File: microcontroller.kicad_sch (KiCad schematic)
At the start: 33 parts, among them J1 Micro_SD_Card, J2 TC2030-NL, J3 USB_C_Receptacle, SW1 SW_SPST, SW2 SW_SPST, U1 W25Q128JVS, U2 STM32F411CEUx, U3 USBLC6-2SC6, Y1 8MHz, Y2 32.768KHz

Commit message: Footprint selection
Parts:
- C1, C10, C11, C12, C2, C3, C4, C5, C6, C7, C8, C9: footprint (none) -> Capacitor_SMD:C_0603_1608Metric
- D1: footprint (none) -> LED_SMD:LED_0603_1608Metric
- D2: footprint (none) -> LED_SMD:LED_RGB_5050-6
- J1: footprint (none) -> Connector_Card:microSD_HC_Molex_47219-2001
- J3: footprint (none) -> Connector_USB:USB_C_Receptacle_GCT_USB4105-xx-A_16P_TopMnt_Horizontal
- R1, R2, R3, R4, R5, R6, R7, R8, R9: footprint (none) -> Resistor_SMD:R_0603_1608Metric
- SW1, SW2: footprint (none) -> Button_Switch_SMD:SW_SPST_B3U-1000P-B
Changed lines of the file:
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@@
 			)
 		)
-		(property "Footprint" ""
+		(property "Footprint" "Capacitor_SMD:C_0603_1608Metric"
 			(at 151.13 40.64 0)
 			(effects
@@
 			)
 		)
-		(property "Footprint" ""
+		(property "Footprint" "Capacitor_SMD:C_0603_1608Metric"
 			(at 157.48 40.64 0)
 			(effects
@@
 			)
 		)
-		(property "Footprint" ""
+		(property "Footprint" "Capacitor_SMD:C_0603_1608Metric"
 			(at 125.73 40.64 0)
 			(effects
@@
 			)
 		)
-		(property "Footprint" ""
+		(property "Footprint" "Capacitor_SMD:C_0603_1608Metric"
 			(at 137.16 144.78 0)
 			(effects
@@
 			)
 		)
-		(property "Footprint" ""
+		(property "Footprint" "Capacitor_SMD:C_0603_1608Metric"
 			(at 119.38 40.64 0)
 			(effects
@@
 			)
 		)
-		(property "Footprint" ""
+		(property "Footprint" "Capacitor_SMD:C_0603_1608Metric"
 			(at 132.08 40.64 0)
 			(effects
@@
 			)
 		)
-		(property "Footprint" ""
+		(property "Footprint" "Resistor_SMD:R_0603_1608Metric"
 			(at 233.934 133.604 90)
 			(effects
@@
 			)
 		)
-		(property "Footprint" ""
+		(property "Footprint" "Capacitor_SMD:C_0603_1608Metric"
 			(at 205.74 92.71 0)
 			(effects
@@
 			)
 		)
-		(property "Footprint" ""
+		(property "Footprint" "Capacitor_SMD:C_0603_1608Metric"
 			(at 205.74 46.99 0)
 			(effects
@@
 			)
 		)
-		(property "Footprint" ""
+		(property "Footprint" "Connector_Card:microSD_HC_Molex_47219-2001"
 			(at 265.43 87.63 0)
 			(effects
@@
 			)
 		)
-		(property "Footprint" ""
+		(property "Footprint" "Resistor_SMD:R_0603_1608Metric"
 			(at 233.934 123.444 90)
 			(effects
@@
 			)
 		)
-		(property "Footprint" ""
+		(property "Footprint" "Button_Switch_SMD:SW_SPST_B3U-1000P-B"
 			(at 35.56 106.68 0)
 			(effects
@@
 			)
 		)
-		(property "Footprint" ""
+		(property "Footprint" "Resistor_SMD:R_0603_1608Metric"
 			(at 113.284 90.424 90)
 			(effects
@@
 			)
 		)
-		(property "Footprint" ""
+		(property "Footprint" "Resistor_SMD:R_0603_1608Metric"
 			(at 37.084 111.506 90)
 			(effects
@@
 			)
 		)
-		(property "Footprint" ""
+		(property "Footprint" "Resistor_SMD:R_0603_1608Metric"
 			(at 52.324 170.434 90)
 			(effects
@@
 			)
 		)
-		(property "Footprint" ""
+		(property "Footprint" "Resistor_SMD:R_0603_1608Metric"
 			(at 251.714 94.234 90)
 			(effects
@@
 			)
 		)
-		(property "Footprint" ""
+		(property "Footprint" "Capacitor_SMD:C_0603_1608Metric"
 			(at 144.78 40.64 0)
 			(effects
@@
 			)
 		)
-		(property "Footprint" ""
+		(property "Footprint" "Button_Switch_SMD:SW_SPST_B3U-1000P-B"
 			(at 38.1 81.28 0)
 			(effects
@@
 			)
 		)
-		(property "Footprint" ""
+		(property "Footprint" "Capacitor_SMD:C_0603_1608Metric"
 			(at 198.12 92.71 0)
 			(effects
@@
 			)
 		)
-		(property "Footprint" ""
+		(property "Footprint" "Resistor_SMD:R_0603_1608Metric"
 			(at 52.324 172.974 90)
 			(effects
@@
 			)
 		)
-		(property "Footprint" ""
+		(property "Footprint" "LED_SMD:LED_RGB_5050-6"
 			(at 242.57 130.81 0)
 			(effects
@@
 			)
 		)
-		(property "Footprint" ""
+		(property "Footprint" "Resistor_SMD:R_0603_1608Metric"
 			(at 251.714 96.774 90)
 			(effects
@@
 			)
 		)
-		(property "Footprint" ""
+		(property "Footprint" "Capacitor_SMD:C_0603_1608Metric"
 			(at 138.43 40.64 0)
 			(effects
@@
 			)
 		)
-		(property "Footprint" ""
+		(property "Footprint" "LED_SMD:LED_0603_1608Metric"
 			(at 120.65 91.44 0)
 			(effects
@@
 			)
 		)
-		(property "Footprint" ""
+		(property "Footprint" "Resistor_SMD:R_0603_1608Metric"
 			(at 233.934 128.524 90)
 			(effects
@@
 			)
 		)
-		(property "Footprint" ""
+		(property "Footprint" "Connector_USB:USB_C_Receptacle_GCT_USB4105-xx-A_16P_TopMnt_Horizontal"
 			(at 36.83 161.29 0)
 			(effects
@@
 			)
 		)
-		(property "Footprint" ""
+		(property "Footprint" "Capacitor_SMD:C_0603_1608Metric"
 			(at 38.1 85.09 0)
 			(effects

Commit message: Connected radio
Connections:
- net EN_RADIO is gone; now on net INT_RADIO: U2.41 (PB5)
- net INT_RADIO: no longer U2.40 (PB4)
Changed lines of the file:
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@@
-		)
-	)
-	(hierarchical_label "INT_RADIO"
-		(shape input)
-		(at 137.16 111.76 180)
-		(effects
-			(font
-				(size 1.27 1.27)
-			)
-			(justify right)
 		)
 	)
@@
 		)
 	)
-	(hierarchical_label "CS_RADIO"
-		(shape output)
-		(at 137.16 119.38 180)
+	(hierarchical_label "INT_RADIO"
+		(shape input)
+		(at 137.16 114.3 180)
 		(effects
 			(font
@@
 		)
 	)
-	(hierarchical_label "EN_RADIO"
+	(hierarchical_label "CS_RADIO"
 		(shape output)
-		(at 137.16 114.3 180)
+		(at 137.16 119.38 180)
 		(effects
 			(font

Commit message: PCB work
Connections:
- net CS_ACCEL: now also U2.20 (PB2); no longer U2.27 (PB14)
- net CS_IMU_AG: now also U2.10 (PA0); no longer U2.25 (PB12)
- net CS_IMU_MAG: now also U2.11 (PA1); no longer U2.26 (PB13)
- net CS_POWER: now also U2.12 (PA2); no longer U2.21 (PB10)
- net CS_RADIO: now also U2.14 (PA4); no longer U2.43 (PB7)
- net INT_RADIO: now also U2.13 (PA3); no longer U2.41 (PB5)
- net LED_BLUE: now also U2.29 (PA8); no longer U2.12 (PA2)
- net LED_GREEN: now also U2.30 (PA9); no longer U2.11 (PA1)
- net LED_RED: now also U2.31 (PA10); no longer U2.10 (PA0)
- net RST_RADIO: now also U2.21 (PB10); no longer U2.42 (PB6)
- no-connect marks 12 -> 13
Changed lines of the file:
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@@
+	)
+	(no_connect
+		(at 137.16 111.76)
+	)
+	(no_connect
+		(at 137.16 119.38)
 	)
 	(no_connect
@@
 	)
 	(no_connect
-		(at 137.16 106.68)
+		(at 137.16 134.62)
 	)
 	(no_connect
@@
 	)
 	(no_connect
-		(at 172.72 81.28)
-	)
-	(no_connect
-		(at 172.72 99.06)
-	)
-	(no_connect
-		(at 172.72 93.98)
+		(at 137.16 129.54)
 	)
 	(no_connect
@@
 	)
 	(no_connect
-		(at 172.72 83.82)
+		(at 137.16 116.84)
 	)
 	(no_connect
-		(at 172.72 96.52)
+		(at 137.16 114.3)
+	)
+	(no_connect
+		(at 137.16 132.08)
 	)
 	(no_connect
@@
 	(wire
 		(pts
+			(xy 181.61 99.06) (xy 172.72 99.06)
+		)
+		(stroke
+			(width 0)
+			(type default)
+		)
+	)
+	(wire
+		(pts
 			(xy 175.26 101.6) (xy 172.72 101.6)
 		)
@@
 	(wire
 		(pts
+			(xy 172.72 93.98) (xy 182.88 93.98)
+		)
+		(stroke
+			(width 0)
+			(type default)
+		)
+	)
+	(wire
+		(pts
+			(xy 184.15 96.52) (xy 172.72 96.52)
+		)
+		(stroke
+			(width 0)
+			(type default)
+		)
+	)
+	(wire
+		(pts
 			(xy 138.43 38.1) (xy 144.78 38.1)
 		)
@@
 	(wire
 		(pts
-			(xy 181.61 73.66) (xy 172.72 73.66)
-		)
-		(stroke
-			(width 0)
-			(type default)
-		)
-	)
-	(wire
-		(pts
 			(xy 40.64 106.68) (xy 40.64 110.49)
 		)
@@
 	(wire
 		(pts
-			(xy 172.72 78.74) (xy 182.88 78.74)
-		)
-		(stroke
-			(width 0)
-			(type default)
-		)
-	)
-	(wire
-		(pts
 			(xy 119.38 43.18) (xy 125.73 43.18)
 		)
@@
 		(pts
 			(xy 132.08 73.66) (xy 137.16 73.66)
-		)
-		(stroke
-			(width 0)
-			(type default)
-		)
-	)
-	(wire
-		(pts
-			(xy 184.15 76.2) (xy 172.72 76.2)
 		)
 		(stroke
@@
 		)
 	)
-	(label "LED_BLUE"
-		(at 182.88 78.74 180)
-		(effects
-			(font
-				(size 1.27 1.27)
-			)
-			(justify right bottom)
-		)
-	)
 	(label "SWD"
 		(at 176.53 106.68 180)
@@
 		)
 	)
-	(label "LED_RED"
-		(at 181.61 73.66 180)
-		(effects
-			(font
-				(size 1.27 1.27)
-			)
-			(justify right bottom)
-		)
-	)
 	(label "MOSI"
 		(at 218.44 100.33 0)
@@
 		)
 	)
-	(label "LED_GREEN"
-		(at 184.15 76.2 180)
-		(effects
-			(font
-				(size 1.27 1.27)
-			)
-			(justify right bottom)
-		)
-	)
 	(label "MISO"
 		(at 218.44 97.79 0)
@@
 		)
 	)
+	(label "LED_BLUE"
+		(at 182.88 93.98 180)
+		(effects
+			(font
+				(size 1.27 1.27)
+			)
+			(justify right bottom)
+		)
+	)
+	(label "LED_RED"
+		(at 181.61 99.06 180)
+		(effects
+			(font
+				(size 1.27 1.27)
+			)
+			(justify right bottom)
+		)
+	)
+	(label "LED_GREEN"
+		(at 184.15 96.52 180)
+		(effects
+			(font
+				(size 1.27 1.27)
+			)
+			(justify right bottom)
+		)
+	)
 	(label "CS_FLASH"
 		(at 217.17 40.64 0)
@@
 			)
 			(justify right bottom)
+		)
+	)
+	(hierarchical_label "CS_IMU_AG"
+		(shape output)
+		(at 172.72 73.66 0)
+		(effects
+			(font
+				(size 1.27 1.27)
+			)
+			(justify left)
+		)
+	)
+	(hierarchical_label "CS_IMU_MAG"
+		(shape output)
+		(at 172.72 76.2 0)
+		(effects
+			(font
+				(size 1.27 1.27)
+			)
+			(justify left)
+		)
+	)
+	(hierarchical_label "CS_RADIO"
+		(shape output)
+		(at 172.72 83.82 0)
+		(effects
+			(font
+				(size 1.27 1.27)
+			)
+			(justify left)
 		)
 	)
@@
 		)
 	)
-	(hierarchical_label "INT_RADIO"
-		(shape input)
-		(at 137.16 114.3 180)
-		(effects
-			(font
-				(size 1.27 1.27)
-			)
-			(justify right)
-		)
-	)
-	(hierarchical_label "CS_RADIO"
-		(shape output)
-		(at 137.16 119.38 180)
-		(effects
-			(font
-				(size 1.27 1.27)
-			)
-			(justify right)
-		)
-	)
 	(hierarchical_label "CS_POWER"
 		(shape output)
-		(at 137.16 127 180)
-		(effects
-			(font
-				(size 1.27 1.27)
-			)
-			(justify right)
-		)
-	)
-	(hierarchical_label "RST_RADIO"
-		(shape output)
-		(at 137.16 116.84 180)
+		(at 172.72 78.74 0)
+		(effects
+			(font
+				(size 1.27 1.27)
+			)
+			(justify left)
+		)
+	)
+	(hierarchical_label "CS_ACCEL"
+		(shape input)
+		(at 137.16 106.68 180)
 		(effects
 			(font
@@
 		)
 	)
-	(hierarchical_label "CS_ACCEL"
-		(shape output)
-		(at 137.16 134.62 180)
-		(effects
-			(font
-				(size 1.27 1.27)
-			)
-			(justify right)
-		)
-	)
-	(hierarchical_label "CS_IMU_MAG"
-		(shape output)
-		(at 137.16 132.08 180)
-		(effects
-			(font
-				(size 1.27 1.27)
-			)
-			(justify right)
+	(hierarchical_label "INT_RADIO"
+		(shape input)
+		(at 172.72 81.28 0)
+		(effects
+			(font
+				(size 1.27 1.27)
+			)
+			(justify left)
 		)
 	)
@@
 		)
 	)
-	(hierarchical_label "CS_IMU_AG"
+	(hierarchical_label "RST_RADIO"
 		(shape output)
-		(at 137.16 129.54 180)
-		(effects
-			(font
+		(at 137.16 127 180)
+		(effects
+			(font

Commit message: Silk updates
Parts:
- added J6: Stemma, Connector_JST:JST_SH_SM04B-SRSS-TB_1x04-1MP_P1.00mm_Horizontal, symbol Connector_Generic_Shielded:Conn_01x04_Shielded
- added R16, R17: 5.1k, Resistor_SMD:R_0603_1608Metric, symbol Device:R_US
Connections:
- net +3V3: now also J6.3 (Pin_3), R16.1, R17.1
- net GND: now also J6.4 (Pin_4), J6.SH (Shield)
- net SCL: now reaches U2.42 (PB6)
- net SCL: now also J6.1 (Pin_1), R16.2
- net SDA: now reaches U2.43 (PB7)
- net SDA: now also J6.2 (Pin_2), R17.2
- no-connect marks 13 -> 11

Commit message: Addeed part numbers
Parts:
- C1, C12: LCSC (none) -> C19666
- C10: LCSC (none) -> C96446
- C11, C3, C4, C5, C6, C7, C8, C9: LCSC (none) -> C14663
- C2: LCSC (none) -> C15849
- D1: LCSC (none) -> C2994781
- D2: LCSC (none) -> C784540
- J1: LCSC (none) -> C164170
- J3: LCSC (none) -> C3025063
- J6: LCSC (none) -> C160404
- R1, R5, R6, R7: LCSC (none) -> C22787
- R16, R17, R8, R9: LCSC (none) -> C2907044
- R2, R3, R4: LCSC (none) -> C98220
- SW1, SW2: LCSC (none) -> C231329
- U1: LCSC (none) -> C97521
- U2: LCSC (none) -> C60420
- U3: LCSC (none) -> C7519
- Y1: LCSC (none) -> ASCO-8.000MHZ-EK-T3
- Y2: footprint Oscillator:Oscillator_SMD_Abracon_ASCO-4Pin_1.6x1.2mm -> Avionics_Feet:OSC_SIT1532AI-J4-DCC-32.768D; LCSC (none) -> C367054
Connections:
- net +3V3: now also Y2.3 (VDD); no longer Y2.1 (Tri-State), Y2.4 (VDD)
- net GND: now also Y2.1 (GND), Y2.4 (GND); no longer Y2.2 (GND)
- net LSE_IN: now also Y2.2 (OUT); no longer Y2.3 (OUT)

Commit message: PCB revisions
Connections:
- net CS_IMU_AG: now also U2.11 (PA1); no longer U2.10 (PA0)
- net CS_IMU_MAG: now also U2.12 (PA2); no longer U2.11 (PA1)
- net CS_POWER: now also U2.10 (PA0); no longer U2.12 (PA2)
- net GND: now also J1.SHIELD (GND); no longer J1.G1 (GND), J1.G2 (GND), J1.G3 (GND), J1.G4 (GND)
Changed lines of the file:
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@@
 	(text "Series resistors\nembeded in USB driver"
 		(exclude_from_sim no)
-		(at 53.086 191.008 0)
+		(at 45.974 188.214 0)
 		(effects
 			(font
@@
 		)
 	)
-	(hierarchical_label "CS_IMU_AG"
-		(shape output)
-		(at 172.72 73.66 0)
-		(effects
-			(font
-				(size 1.27 1.27)
-			)
-			(justify left)
-		)
-	)
 	(hierarchical_label "CS_IMU_MAG"
 		(shape output)
-		(at 172.72 76.2 0)
+		(at 172.72 78.74 0)
 		(effects
 			(font
@@
 	(hierarchical_label "CS_POWER"
 		(shape output)
-		(at 172.72 78.74 0)
+		(at 172.72 73.66 0)
 		(effects
 			(font
@@
 		)
 	)
+	(hierarchical_label "CS_IMU_AG"
+		(shape output)
+		(at 172.72 76.2 0)
+		(effects
+			(font
+				(size 1.27 1.27)
+			)
+			(justify left)
+		)
+	)
 	(symbol
 		(lib_id "power:+3V3")
@@
 		(pin "4"
 		)
-		(pin "G4"
+		(pin "SHIELD"
 		)
 		(pin "5"
@@
 		(pin "7"
 		)
-		(pin "G1"
+		(pin "SHIELD"
 		)
-		(pin "G2"
+		(pin "SHIELD"
 		)
-		(pin "G3"
+		(pin "SHIELD"
 		)
 		(pin "6"
@@
 			)
 		)
-		(property "Datasheet" "https://abracon.com/Oscillators/ASCO.pdf"
+		(property "Datasheet" "https://www.lcsc.com/datasheet/C367054.pdf"
 			(at 75.565 97.155 0)
 			(effects
@@
 			)
 		)
-		(property "Description" "Crystal Clock Oscillator, Abracon ASCO"
+		(property "Description" "SiT1552"
 			(at 81.28 100.33 0)
 			(effects

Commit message: Added Digikey Components
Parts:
- D1: Digikey (none) -> LTST-C191KGKT
- D2: Digikey (none) -> 150505M173300
- J1: Digikey (none) -> 0472192001
- J3: Digikey (none) -> USB4105-GF-A
- J6: Digikey (none) -> SM04B-SRSS-TB
- SW1, SW2: Digikey (none) -> B3U-1000P-B
- U1: Digikey (none) -> W25Q128JVSIM TR
- U2: Digikey (none) -> STM32F411CEU6
- U3: Digikey (none) -> USBLC6-2SC6
- Y1: Digikey (none) -> ASCO-8.000MHZ-EK-T3
- Y2: value 32.768KHz -> 32.768kHz; footprint Avionics_Feet:OSC_SIT1532AI-J4-DCC-32.768D -> Oscillator:Oscillator_SMD_Abracon_ASCO-4Pin_1.6x1.2mm; Digikey (none) -> 50-ECS-327MV-CN-TRCT-ND; LCSC C367054 -> (none)
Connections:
- net +3V3: now also Y2.1 (Tri-State), Y2.4 (VDD); no longer Y2.3 (VDD)
- net GND: now also Y2.2 (GND); no longer Y2.1 (GND), Y2.4 (GND)
- net LSE_IN: now also Y2.3 (OUT); no longer Y2.2 (OUT)

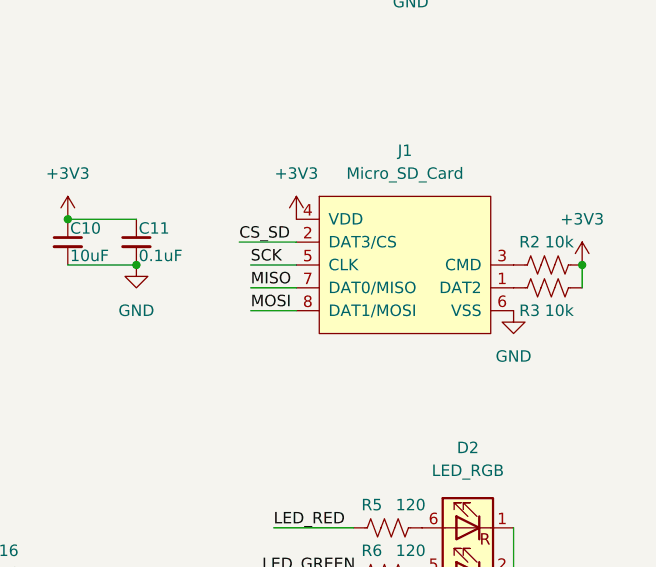
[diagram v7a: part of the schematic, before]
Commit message: Updated SD card to corrected symbol
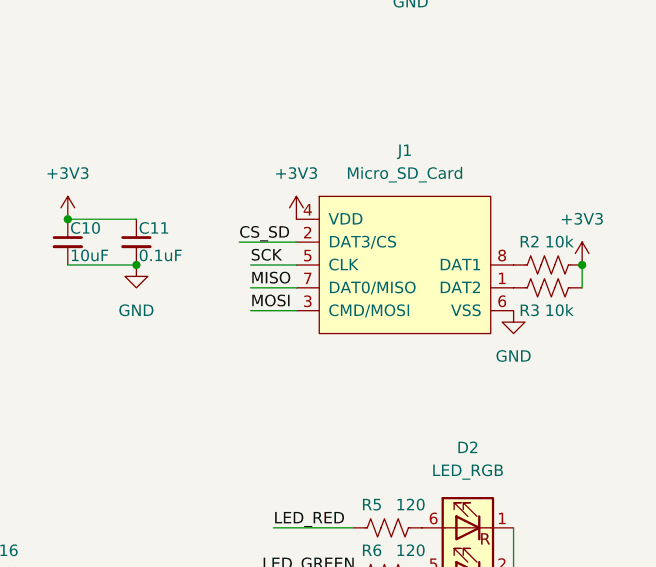
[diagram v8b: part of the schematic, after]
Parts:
- J1: Digikey 0472192001 -> (none); LCSC C164170 -> (none)
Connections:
- net MOSI: now also J1.3 (CMD/MOSI); no longer J1.8 (DAT1/MOSI)
- net at R2.1: now also J1.8 (DAT1); no longer J1.3 (CMD)
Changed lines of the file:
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@@
 			)
-		)
-		(property "LCSC" "C164170"
-			(at 236.22 95.25 0)
-			(effects
-				(font
-					(size 1.27 1.27)
-				)
-				(hide yes)
-			)
-		)
-		(property "Digikey" "0472192001"
-			(at 236.22 95.25 0)
-			(effects
-				(font
-					(size 1.27 1.27)
-				)
-				(hide yes)
-			)
-		)
-		(pin "2"
-		)
-		(pin "3"
-		)
-		(pin "4"
-		)
-		(pin "SHIELD"
-		)
-		(pin "5"
 		)
 		(pin "1"
 		)
 		(pin "8"
+		)
+		(pin "6"
 		)
 		(pin "7"
@@
 		(pin "SHIELD"
 		)
+		(pin "4"
+		)
+		(pin "2"
+		)
 		(pin "SHIELD"
 		)
-		(pin "6"
+		(pin "3"
+		)
+		(pin "5"
+		)
+		(pin "SHIELD"
 		)
 		(instances
